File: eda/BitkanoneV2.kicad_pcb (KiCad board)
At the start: 2 copper layers, 131 parts, among them J211 JH23, J212 JL23, J231 Jumper, J232 Jumper, J233 Jumper, J234 Jumper, Q501 PH_NPN, Q502 PH_NPN, U201 BluePill_STM32F103C, U202 MCP2551-I-SN, U301 6DOF, X101 01x02M, X102 01x02M, X200 01x03M, X201 5VUSB, X231 Bus, X232 Bus, X233 Bus, X234 Bus, X401 MotorCon, X42 Conn_01x07_Male, X990 Conn_01x01, X991 Conn_01x01

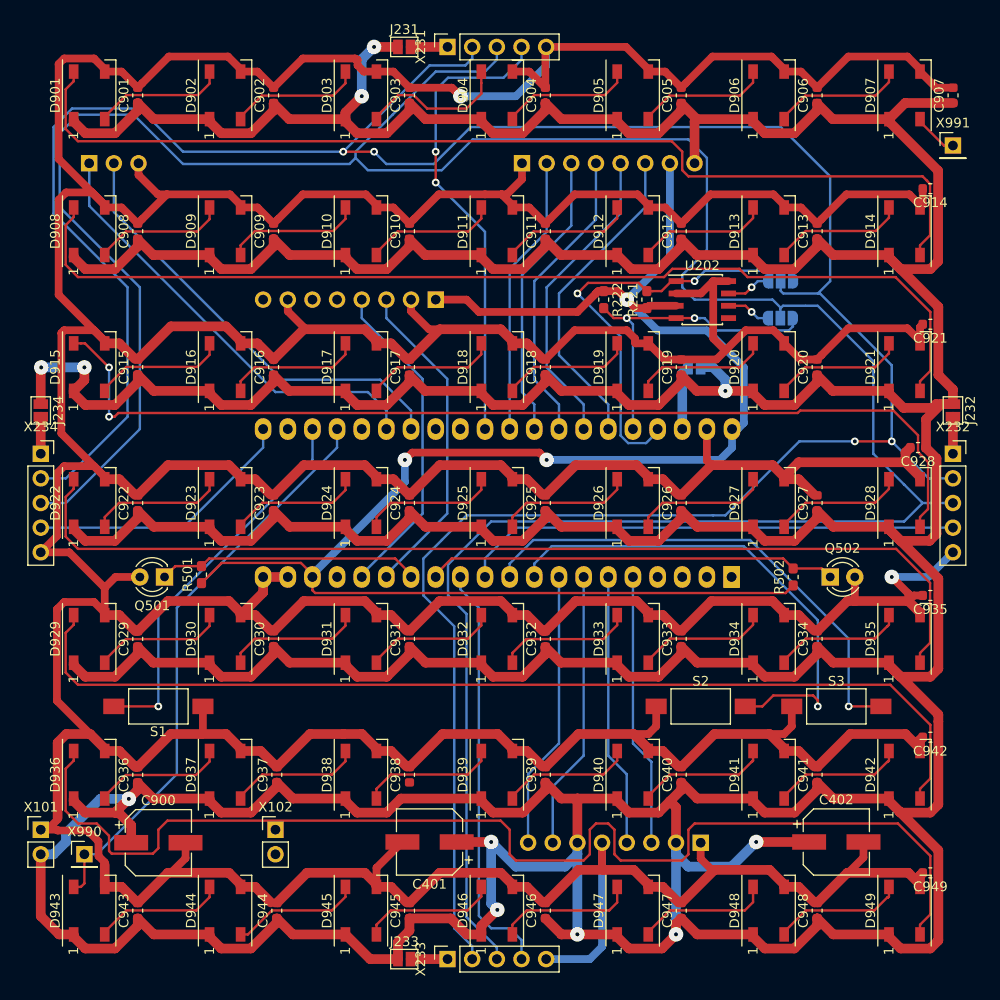
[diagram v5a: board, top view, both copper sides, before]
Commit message: silk screen documentation added
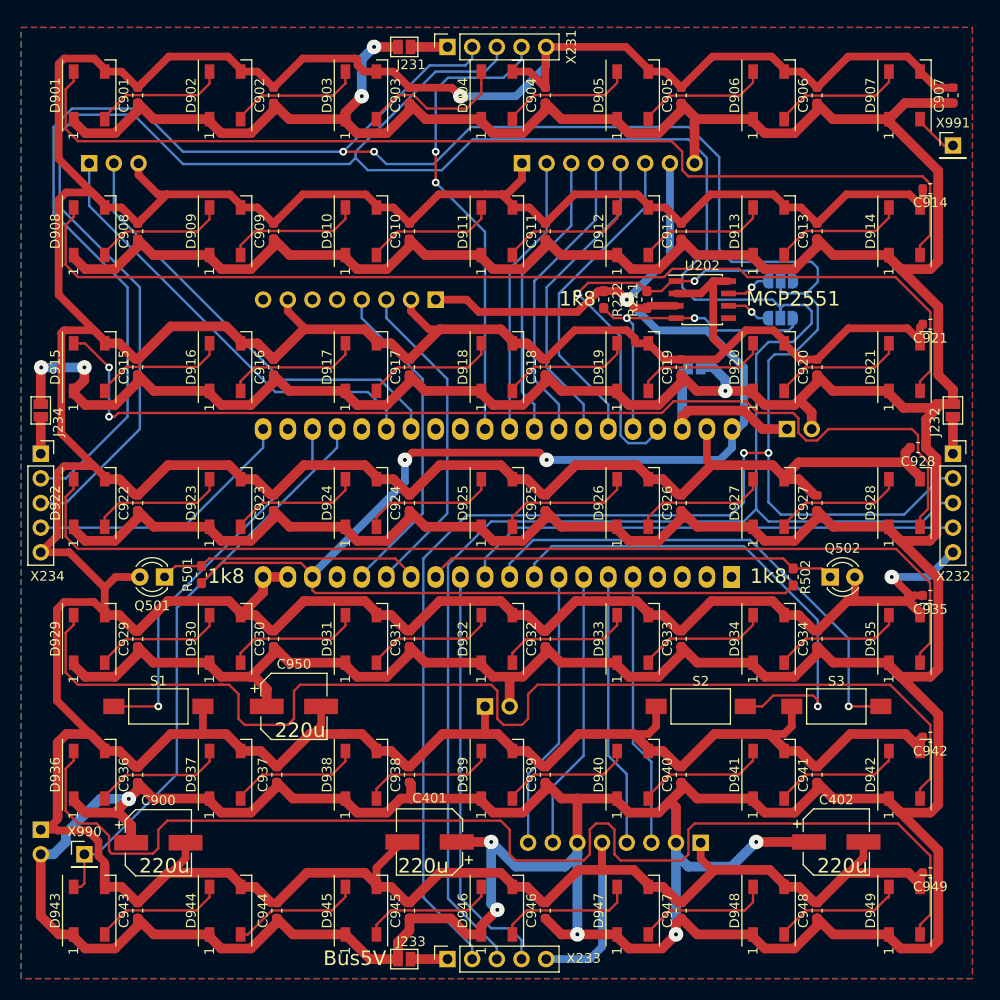
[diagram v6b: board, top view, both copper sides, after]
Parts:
- added C950: 220u, Capacitor_SMD:CP_Elec_6.3x5.3, F.Cu at (48.1, 90.0)
- added J202: 5VUSB, Connector_PinSocket_2.54mm:PinSocket_1x02_P2.54mm_Vertical, B.Cu at (98.9, 61.4)
- added bitkanoneV2: Symbol_GNU-Logo_SilkscreenTop, Symbol:Symbol_GNU-Logo_SilkscreenTop, B.Cu at (46.8, 95.1)
- X101, X102: moved to B.Cu
- moved X102 25.0 mm to (67.8, 90.0), turned to 270 degrees
- turned X101 to 180 degrees
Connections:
- net Net-(U201-Pad26) renamed /TX1
- net Net-(U201-Pad27) renamed /RX1
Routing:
- net Net-(D929-Pad4): track 105.6 -> 119.1 mm
- net Net-(J202-Pad1): track 6.63 -> 19.7 mm
- net +5V: track 981.4 -> 993.7 mm
- net /CANH: track 290.4 -> 297.7 mm
- net GND: track 973.1 -> 979.9 mm
- net Net-(D915-Pad4): track 104.9 -> 107.5 mm
- net /CANL: track 292.7 -> 293.9 mm
- added copper zone on B.Cu, net GND
- added copper zone on F.Cu, net GND
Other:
- board text added: "+3V3"
- board text added: "+5V"
- board text added: "-"
- board text added: "1k8"
- board text added: "220u"
- board text added: "5V+"
- board text added: "5VUSB"
- board text added: "AD0"
- board text added: "Bus5V"
- board text added: "Bus:"
- board text added: "CAN"
- board text added: "CANH"
- board text added: "CANL"
- board text added: "Din"
- board text added: "Dout"
- board text added: "EN"
- board text added: "I2C"
- board text added: "MCP2551"
- board text added: "MPU6050 6DOF"
- board text added: "PB3"
- board text added: "PB4"
- board text added: "PB5"
- board text added: "PB6 SCL1"
- board text added: "PB7 SDA1"
- board text added: "PWM"
- board text added: "RX"
- board text added: "SCL"
- board text added: "SDA"
- board text added: "Servo1"
- board text added: "Servo2"
- board text added: "TOPO"
- board text added: "TX"
- board text added: "forth-ev.de"
- board text added: "github.com/GeraldWodni/bitkanoneV2"

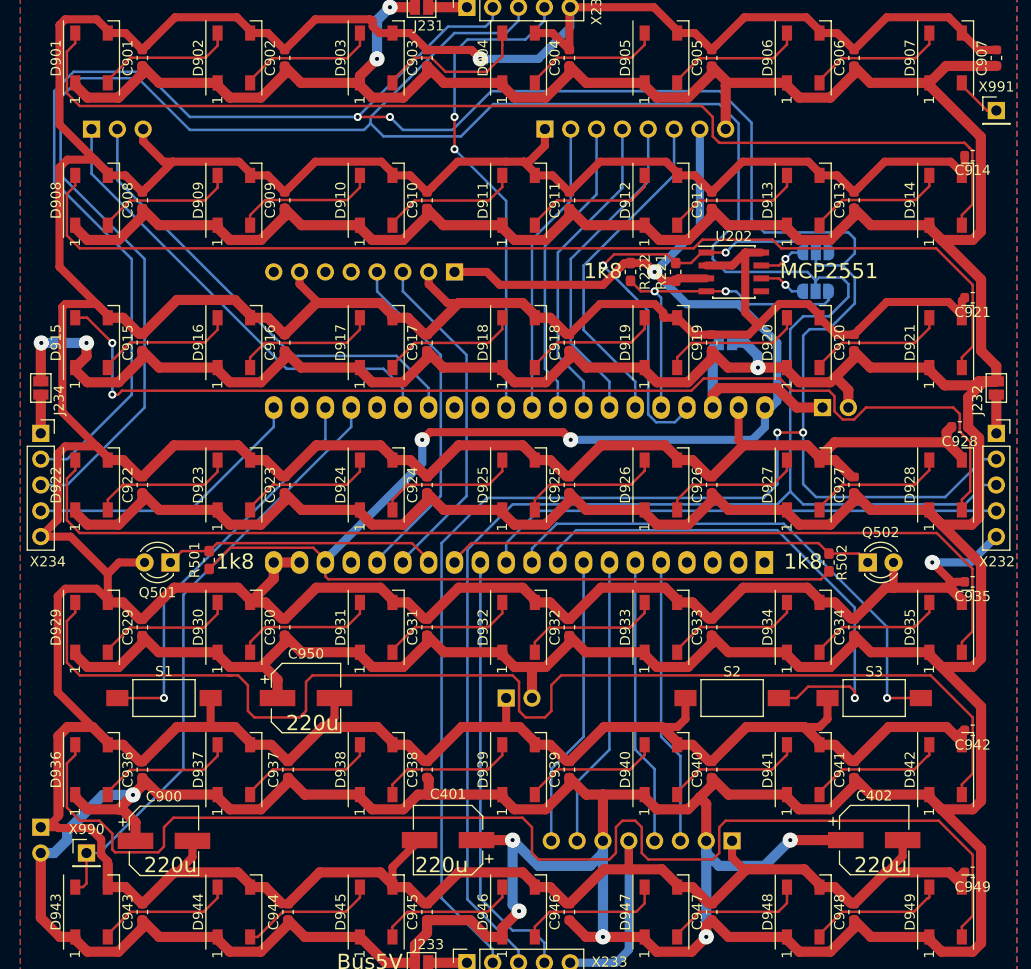
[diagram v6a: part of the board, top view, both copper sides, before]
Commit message: USB port added; Mounting holes added; Silk screen measurements added
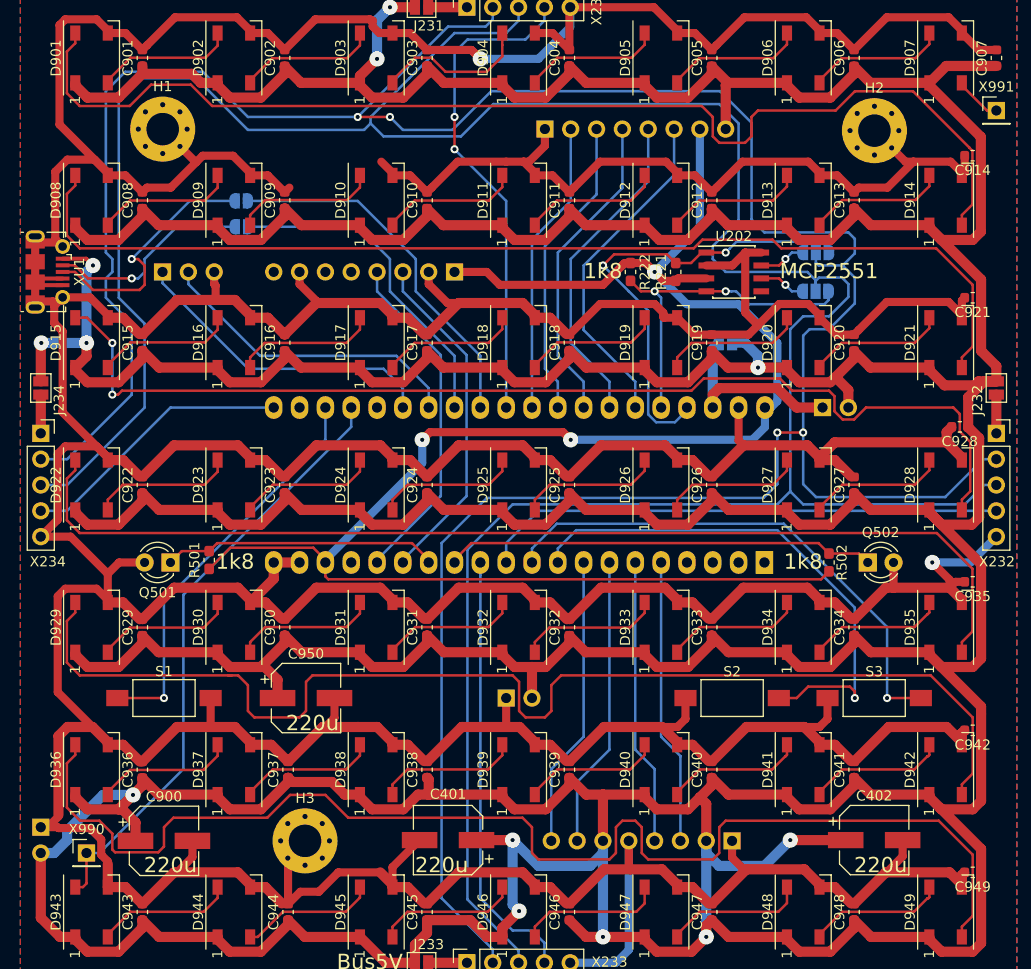
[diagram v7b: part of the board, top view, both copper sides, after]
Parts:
- added H1: MountingHole_Pad, MountingHole:MountingHole_3.2mm_M3_Pad_Via, F.Cu at (34.0, 34.0)
- added H2: MountingHole_Pad, MountingHole:MountingHole_3.2mm_M3_Pad_Via, F.Cu at (104.0, 34.1)
- added H3: MountingHole_Pad, MountingHole:MountingHole_3.2mm_M3_Pad_Via, F.Cu at (48.0, 104.0)
- added JU1: Jumper, Jumper:SolderJumper-2_P1.3mm_Open_RoundedPad1.0x1.5mm, B.Cu at (41.7, 41.1)
- added JU2: Jumper, Jumper:SolderJumper-2_P1.3mm_Open_RoundedPad1.0x1.5mm, B.Cu at (41.7, 43.6)
- added XU1: USB_B_Micro, Connector_USB:USB_Micro-B_Molex-105017-0001, F.Cu at (22.7, 48.0)
- bitkanoneV2: value Symbol_GNU-Logo_SilkscreenTop -> GNU Logo
- moved X200 15.7 mm to (34.0, 48.0)
- moved bitkanoneV2 5.75 mm to (47.5, 89.4)
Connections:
- U201 pad 28: Net-(U201-Pad28) -> /USBD-
- U201 pad 29: Net-(U201-Pad29) -> /USBD+
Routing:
- net /USBD+: track 0.00 -> 36.1 mm
- net /USBD-: track 0.00 -> 32.5 mm
- net Net-(JU1-Pad1): track 0.00 -> 24.9 mm, vias 0 -> 1
- net Net-(JU2-Pad1): track 0.00 -> 20.3 mm, vias 0 -> 1
- net GND: track 979.9 -> 996.1 mm
- net /RX1: track 46.0 -> 31.0 mm
- net /TX1: track 45.6 -> 30.9 mm
- net +5V: track 993.7 -> 1004.5 mm, vias 11 -> 12
- net /CANL: track 293.9 -> 285.9 mm
- net Net-(D901-Pad4): track 106.5 -> 113.6 mm
- net /CANH: track 297.7 -> 291.0 mm
- net Net-(D936-Pad4): track 123.4 -> 125.3 mm
- net /TLeft: track 28.2 -> 27.1 mm
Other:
- board text added: "14mm"
- board text added: "28mm"
- board text added: "98mm"
- board text added: "="
